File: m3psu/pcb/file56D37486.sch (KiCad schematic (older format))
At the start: 42 parts

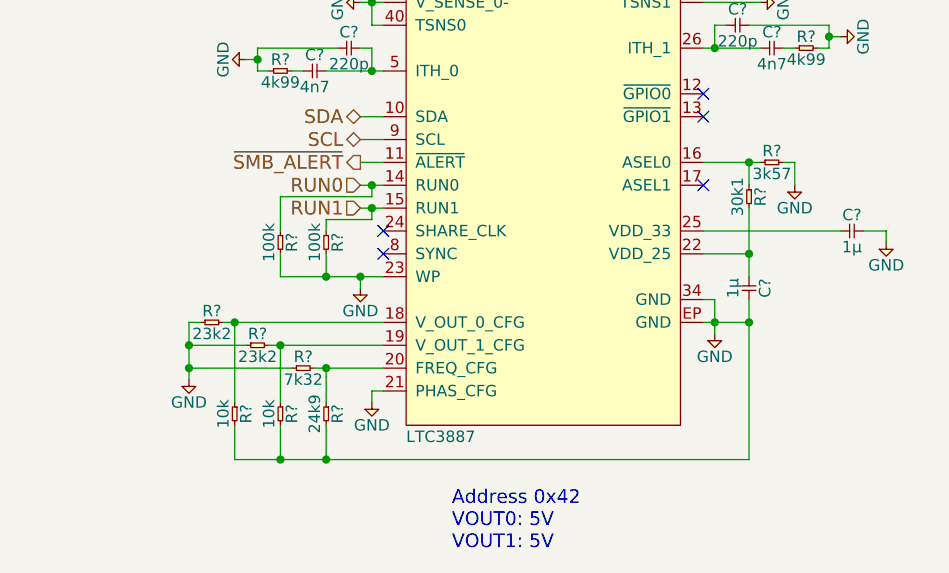
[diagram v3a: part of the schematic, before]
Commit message: Added current monitor and control for pyros. Modified DC/DC converters.
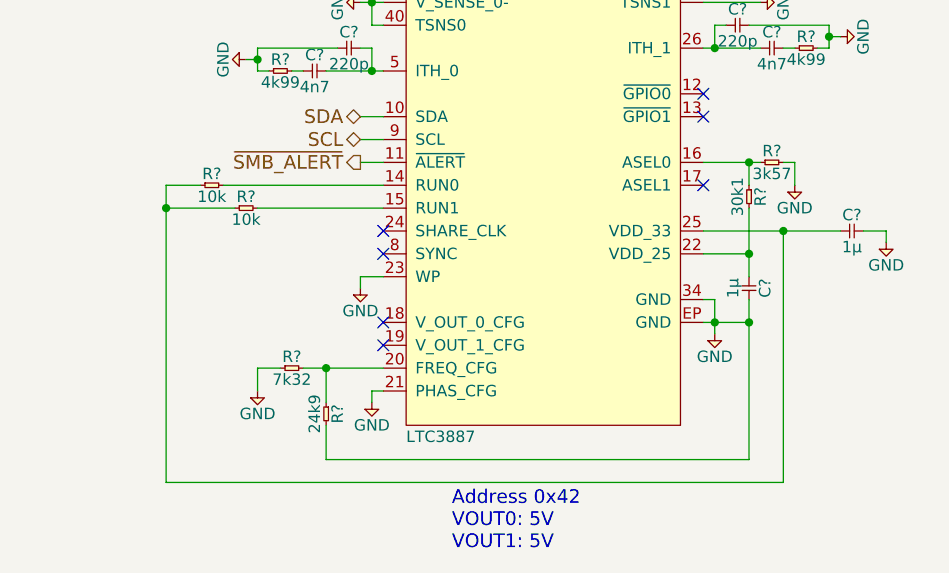
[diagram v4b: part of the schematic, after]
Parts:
- removed R?: 24k9, agg:0402, symbol R
- removed R? (x2): 10k, agg:0402, symbol R
- removed R? (x2): 23k2, agg:0402, symbol R
- removed R?: 7k32, agg:0402, symbol R
- removed R? (x2): 100k, agg:0402, symbol R
- added R?: 24k9, agg:0402, symbol R
- added R?: 7k32, agg:0402, symbol R
- added R? (x2): 10k, agg:0402, symbol R
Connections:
- net GND: now also R?.1, R?.2
- net at IC?.20 (FREQ_CFG): now also R?.1, R?.2
- net at C?.1, IC?.25 (VDD_33): now also R?.1, R?.1
- net RUN0: no longer names the net of IC?.14 (RUN0)
- net RUN0: now also R?.2
- net RUN1: no longer names the net of IC?.15 (RUN1)
- net RUN1: now also R?.2
- no-connect marks 5 -> 7
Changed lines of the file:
@@
 $Descr A4 11693 8268
 encoding utf-8
-Sheet 7 10
+Sheet 7 12
 Title ""
 Date ""
@@
 	1    0    0    -1
 $EndComp
-$Comp
-L R R?
-U 1 1 56D56E95
-P 4850 5300
-F 0 "R?" H 4900 5350 50  0000 C CNN
-F 1 "24k9" H 4900 5250 50  0000 C CNN
-F 2 "agg:0402" H 4850 5300 50  0001 C CNN
-F 3 "" H 4850 5300 50  0001 C CNN
-F 4 "1803690" H 4850 5300 60  0001 C CNN "Farnell"
-	1    4850 5300
-	0    1    1    0
-$EndComp
-$Comp
-L R R?
-U 1 1 56D56E9D
-P 4650 5300
-F 0 "R?" H 4700 5350 50  0000 C CNN
-F 1 "10k" H 4700 5250 50  0000 C CNN
-F 2 "agg:0402" H 4650 5300 50  0001 C CNN
-F 3 "" H 4650 5300 50  0001 C CNN
-F 4 "2447096" H 4650 5300 60  0001 C CNN "Farnell"
-	1    4650 5300
-	0    1    1    0
-$EndComp
-$Comp
-L R R?
-U 1 1 56D56EA5
-P 4450 5300
-F 0 "R?" H 4500 5350 50  0000 C CNN
-F 1 "10k" H 4500 5250 50  0000 C CNN
-F 2 "agg:0402" H 4450 5300 50  0001 C CNN
-F 3 "" H 4450 5300 50  0001 C CNN
-F 4 "2447096" H 4450 5300 60  0001 C CNN "Farnell"
-	1    4450 5300
-	0    1    1    0
-$EndComp
-$Comp
-L R R?
-U 1 1 56D56EAD
-P 4300 4950
-F 0 "R?" H 4350 5000 50  0000 C CNN
-F 1 "23k2" H 4350 4900 50  0000 C CNN
-F 2 "agg:0402" H 4300 4950 50  0001 C CNN
-F 3 "" H 4300 4950 50  0001 C CNN
-F 4 "2302774" H 4300 4950 60  0001 C CNN "Farnell"
-	1    4300 4950
-	1    0    0    -1
-$EndComp
-$Comp
-L R R?
-U 1 1 56D56EB5
-P 4500 5050
-F 0 "R?" H 4550 5100 50  0000 C CNN
-F 1 "23k2" H 4550 5000 50  0000 C CNN
-F 2 "agg:0402" H 4500 5050 50  0001 C CNN
-F 3 "" H 4500 5050 50  0001 C CNN
-F 4 "2302774" H 4500 5050 60  0001 C CNN "Farnell"
-	1    4500 5050
-	1    0    0    -1
-$EndComp
-$Comp
-L R R?
-U 1 1 56D56EBD
-P 4700 5150
-F 0 "R?" H 4750 5200 50  0000 C CNN
-F 1 "7k32" H 4750 5100 50  0000 C CNN
-F 2 "agg:0402" H 4700 5150 50  0001 C CNN
-F 3 "" H 4700 5150 50  0001 C CNN
-F 4 "2073231" H 4700 5150 60  0001 C CNN "Farnell"
-	1    4700 5150
-	1    0    0    -1
-$EndComp
-$Comp
-L GND #PWR?
-U 1 1 56D56EC4
-P 4250 5200
-F 0 "#PWR?" H 4120 5240 50  0001 L CNN
-F 1 "GND" H 4250 5100 50  0000 C CNN
-F 2 "" H 4250 5200 60  0000 C CNN
-F 3 "" H 4250 5200 60  0000 C CNN
-	1    4250 5200
-	1    0    0    -1
-$EndComp
 Text HLabel 5000 4050 0    60   BiDi ~ 0
 SDA
 Text HLabel 5000 4150 0    60   BiDi ~ 0
 SCL
-Text HLabel 5000 4350 0    60   Input ~ 0
-RUN0
-Text HLabel 5000 4450 0    60   Input ~ 0
-RUN1
 $Comp
 L GND #PWR?
@@
 	5000 3750 5050 3750
 Wire Wire Line
-	5050 4500 5050 4450
-Wire Wire Line
 	7050 3650 6700 3650
 Connection ~ 7050 3700
@@
 Wire Wire Line
 	6500 3750 6750 3750
-Connection ~ 5050 4450
-Connection ~ 5050 4350
-Wire Wire Line
-	5050 4400 5050 4350
 Wire Wire Line
 	5000 4150 5100 4150
 Wire Wire Line
 	5000 4050 5100 4050
-Wire Wire Line
-	5000 4350 5100 4350
-Wire Wire Line
-	5000 4450 5100 4450
 Wire Wire Line
 	6850 4250 6900 4250
@@
 	5000 4750 5000 4800
 Wire Wire Line
-	4650 4750 5100 4750
-Connection ~ 4250 5150
-Wire Wire Line
-	4250 5150 4700 5150
-Connection ~ 4250 5050
-Wire Wire Line
-	4500 5050 4250 5050
-Wire Wire Line
-	4250 4950 4250 5200
-Wire Wire Line
-	4300 4950 4250 4950
-Connection ~ 4850 5150
-Connection ~ 4650 5050
-Connection ~ 4450 4950
-Wire Wire Line
-	4400 4950 5100 4950
-Wire Wire Line
-	4450 5300 4450 4950
-Wire Wire Line
-	4600 5050 5100 5050
-Wire Wire Line
-	4650 5300 4650 5050
-Wire Wire Line
-	4800 5150 5100 5150
-Wire Wire Line
-	4850 5150 4850 5300
-Wire Wire Line
 	5050 5250 5100 5250
-Connection ~ 4850 5550
-Wire Wire Line
-	4850 5400 4850 5550
-Connection ~ 4650 5550
-Wire Wire Line
-	4650 5400 4650 5550
-Wire Wire Line
-	4450 5550 4450 5400
 Connection ~ 6700 4950
-Wire Wire Line
-	6700 5550 4450 5550
 Wire Wire Line
 	7200 4550 7300 4550
@@
 Text Notes 5400 5950 0    60   ~ 0
 Address 0x42\nVOUT0: 5V\nVOUT1: 5V
-$Comp
-L R R?
-U 1 1 56D56FDB
-P 4850 4550
-F 0 "R?" H 4900 4600 50  0000 C CNN
-F 1 "100k" H 4900 4500 50  0000 C CNN
-F 2 "agg:0402" H 4850 4550 50  0001 C CNN
-F 3 "" H 4850 4550 50  0001 C CNN
-F 4 "2447094" H 4850 4550 60  0001 C CNN "Farnell"
-	1    4850 4550
-	0    1    1    0
-$EndComp
-Wire Wire Line
-	4850 4750 4850 4650
-Connection ~ 5000 4750
-Wire Wire Line
-	5050 4500 4850 4500
-Wire Wire Line
-	4850 4500 4850 4550
-Wire Wire Line
-	5050 4400 4650 4400
-Wire Wire Line
-	4650 4400 4650 4550
-$Comp
-L R R?
-U 1 1 56D56FE9
-P 4650 4550
-F 0 "R?" H 4700 4600 50  0000 C CNN
-F 1 "100k" H 4700 4500 50  0000 C CNN
-F 2 "agg:0402" H 4650 4550 50  0001 C CNN
-F 3 "" H 4650 4550 50  0001 C CNN
-F 4 "2447094" H 4650 4550 60  0001 C CNN "Farnell"
-	1    4650 4550
-	0    1    1    0
-$EndComp
-Wire Wire Line
-	4650 4650 4650 4750
-Connection ~ 4850 4750
+Wire Wire Line
+	5000 4750 5100 4750
+$Comp
+L R R?
+U 1 1 56DDC75E
+P 4850 5300
+F 0 "R?" H 4900 5350 50  0000 C CNN
+F 1 "24k9" H 4900 5250 50  0000 C CNN
+F 2 "agg:0402" H 4850 5300 50  0001 C CNN
+F 3 "" H 4850 5300 50  0001 C CNN
+F 4 "1803690" H 4850 5300 60  0001 C CNN "Farnell"
+	1    4850 5300
+	0    1    1    0
+$EndComp
+$Comp
+L GND #PWR?
+U 1 1 56DDC765
+P 4550 5250
+F 0 "#PWR?" H 4420 5290 50  0001 L CNN
+F 1 "GND" H 4550 5150 50  0000 C CNN
+F 2 "" H 4550 5250 60  0000 C CNN
+F 3 "" H 4550 5250 60  0000 C CNN
+	1    4550 5250
+	1    0    0    -1
+$EndComp
+Connection ~ 4850 5150
+Wire Wire Line
+	4750 5150 5100 5150
+Wire Wire Line
+	4850 5150 4850 5300
+Wire Wire Line
+	4850 5400 4850 5550
+$Comp
+L R R?
+U 1 1 56DDC770
+P 4650 5150
+F 0 "R?" H 4700 5200 50  0000 C CNN
+F 1 "7k32" H 4700 5100 50  0000 C CNN
+F 2 "agg:0402" H 4650 5150 50  0001 C CNN
+F 3 "" H 4650 5150 50  0001 C CNN
+F 4 "2073231" H 4650 5150 60  0001 C CNN "Farnell"
+	1    4650 5150
+	1    0    0    -1
+$EndComp
+Wire Wire Line
+	4650 5150 4550 5150
+Wire Wire Line
+	4550 5150 4550 5250
+Wire Wire Line
+	4850 5550 6700 5550
+Wire Wire Line
+	4150 5650 6850 5650
+Wire Wire Line
+	4150 4350 4150 5650
+$Comp
+L R R?
+U 1 1 56DDC77D
+P 4300 4350
+F 0 "R?" H 4350 4400 50  0000 C CNN
+F 1 "10k" H 4350 4300 50  0000 C CNN
+F 2 "agg:0402" H 4300 4350 50  0001 C CNN
+F 3 "" H 4300 4350 50  0001 C CNN
+F 4 "2447096" H 4300 4350 60  0001 C CNN "Farnell"
+	1    4300 4350
+	1    0    0    -1
+$EndComp
+$Comp
+L R R?
+U 1 1 56DDC785
+P 4450 4450
+F 0 "R?" H 4500 4500 50  0000 C CNN
+F 1 "10k" H 4500 4400 50  0000 C CNN
+F 2 "agg:0402" H 4450 4450 50  0001 C CNN
+F 3 "" H 4450 4450 50  0001 C CNN
+F 4 "2447096" H 4450 4450 60  0001 C CNN "Farnell"
+	1    4450 4450
+	1    0    0    -1
+$EndComp
+Wire Wire Line
+	4150 4350 4300 4350
+Wire Wire Line
+	4450 4450 4150 4450
+Connection ~ 4150 4450
+Wire Wire Line
+	4400 4350 5100 4350
+Wire Wire Line
+	4550 4450 5100 4450
+Wire Wire Line
+	6850 5650 6850 4550
+Connection ~ 6850 4550
+NoConn ~ 5100 4950
+NoConn ~ 5100 5050
 $EndSCHEMATC

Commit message: Added footprints and datasheets to ALL transistors. Only 47uF capacitor has no footprint now.
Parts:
- removed Q? (x4): NFET, symbol NFET
- added Q? (x4): SiZ340DT, agg:PowerPair3x3, symbol SiZ340DT
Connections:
- net GND: now also Q?.S2, Q?.S2
- net VCC: now also Q?.D1 (S1D2), Q?.D1 (S1D2)
- net at C?.2, IC?.29 (SW1), L?.1: now also Q?.S1D2, Q?.S1D2
- net at IC?.30 (TG1): now also Q?.G1
- net at IC?.32 (BG1): now also Q?.G2
- net at IC?.36 (BG0): now also Q?.G2
- net at IC?.38 (TG0): now also Q?.G1
- net at C?.1, IC?.39 (SW0), L?.2: now also Q?.S1D2, Q?.S1D2
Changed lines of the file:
@@
-$EndComp
-$Comp
-L NFET Q?
-U 1 1 56D56D8B
-P 7150 2650
-F 0 "Q?" H 6900 2680 50  0000 L CNN
-F 1 "NFET" H 6900 2490 50  0000 L CNN
-F 2 "" H 7150 2650 50  0001 C CNN
-F 3 "" H 7150 2650 50  0001 C CNN
-F 4 "2422226" H 7150 2650 60  0001 C CNN "Farnell"
-	1    7150 2650
-	1    0    0    -1
-$EndComp
-$Comp
-L NFET Q?
-U 1 1 56D56D93
-P 7150 3050
-F 0 "Q?" H 6900 3080 50  0000 L CNN
-F 1 "NFET" H 6900 2890 50  0000 L CNN
-F 2 "" H 7150 3050 50  0001 C CNN
-F 3 "" H 7150 3050 50  0001 C CNN
-F 4 "2422226" H 7150 3050 60  0001 C CNN "Farnell"
-	1    7150 3050
-	1    0    0    -1
-$EndComp
-$Comp
-L NFET Q?
-U 1 1 56D56D9B
-P 4450 3050
-F 0 "Q?" H 4200 3080 50  0000 L CNN
-F 1 "NFET" H 4200 2890 50  0000 L CNN
-F 2 "" H 4450 3050 50  0001 C CNN
-F 3 "" H 4450 3050 50  0001 C CNN
-F 4 "2422226" H 4450 3050 60  0001 C CNN "Farnell"
-	1    4450 3050
-	-1   0    0    -1
-$EndComp
-$Comp
-L NFET Q?
-U 1 1 56D56DA3
-P 4450 2650
-F 0 "Q?" H 4200 2680 50  0000 L CNN
-F 1 "NFET" H 4200 2490 50  0000 L CNN
-F 2 "" H 4450 2650 50  0001 C CNN
-F 3 "" H 4450 2650 50  0001 C CNN
-F 4 "2422226" H 4450 2650 60  0001 C CNN "Farnell"
-	1    4450 2650
-	-1   0    0    -1
 $EndComp
 $Comp
@@
 NoConn ~ 5100 4950
 NoConn ~ 5100 5050
+$Comp
+L SiZ340DT Q?
+U 1 1 56E08906
+P 7150 2650
+AR Path="/56B7662E/56B76640/56E08906" Ref="Q?"  Part="1"
+AR Path="/56B7662E/56D37487/56E08906" Ref="Q?"  Part="1"
+F 0 "Q?" H 6900 2700 50  0000 L CNN
+F 1 "SiZ340DT" H 7200 2550 50  0000 L CNN
+F 2 "agg:PowerPair3x3" H 7150 2350 50  0001 C CNN
+F 3 "http://www.vishay.com/docs/62877/siz340dt.pdf" H 6900 2700 50  0001 C CNN
+F 4 "2422226" H 7100 2850 50  0001 C CNN "Farnell"
+	1    7150 2650
+	1    0    0    -1
+$EndComp
+$Comp
+L SiZ340DT Q?
+U 2 1 56E0890E
+P 7150 3050
+AR Path="/56B7662E/56B76640/56E0890E" Ref="Q?"  Part="2"
+AR Path="/56B7662E/56D37487/56E0890E" Ref="Q?"  Part="2"
+F 0 "Q?" H 6900 3100 50  0000 L CNN
+F 1 "SiZ340DT" H 7200 2950 50  0000 L CNN
+F 2 "agg:PowerPair3x3" H 7150 2750 50  0001 C CNN
+F 3 "http://www.vishay.com/docs/62877/siz340dt.pdf" H 6900 3100 50  0001 C CNN
+F 4 "2422226" H 7100 3250 50  0001 C CNN "Farnell"
+	2    7150 3050
+	1    0    0    -1
+$EndComp
+$Comp
+L SiZ340DT Q?
+U 1 1 56E08A62
+P 4450 2650
+AR Path="/56B7662E/56B76640/56E08A62" Ref="Q?"  Part="1"
+AR Path="/56B7662E/56D37487/56E08A62" Ref="Q?"  Part="1"
+F 0 "Q?" H 4200 2700 50  0000 L CNN
+F 1 "SiZ340DT" H 4500 2550 50  0000 L CNN
+F 2 "agg:PowerPair3x3" H 4450 2350 50  0001 C CNN
+F 3 "http://www.vishay.com/docs/62877/siz340dt.pdf" H 4200 2700 50  0001 C CNN
+F 4 "2422226" H 4400 2850 50  0001 C CNN "Farnell"
+	1    4450 2650
+	-1   0    0    -1
+$EndComp
+$Comp
+L SiZ340DT Q?
+U 2 1 56E08A6A
+P 4450 3050
+AR Path="/56B7662E/56B76640/56E08A6A" Ref="Q?"  Part="2"
+AR Path="/56B7662E/56D37487/56E08A6A" Ref="Q?"  Part="2"
+F 0 "Q?" H 4200 3100 50  0000 L CNN
+F 1 "SiZ340DT" H 4500 2950 50  0000 L CNN
+F 2 "agg:PowerPair3x3" H 4450 2750 50  0001 C CNN
+F 3 "http://www.vishay.com/docs/62877/siz340dt.pdf" H 4200 3100 50  0001 C CNN
+F 4 "2422226" H 4400 3250 50  0001 C CNN "Farnell"
+	2    4450 3050
+	-1   0    0    -1
+$EndComp
 $EndSCHEMATC

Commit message: Added in PSU for PSU. Updated README.md. Not sure what's this m3psu-rescue.lib is for...
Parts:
- C? (x3): footprint agg:0603 -> agg:0805; Farnell 2494232 -> 1907510
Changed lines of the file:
@@
 EESchema Schematic File Version 2
+LIBS:m3psu-rescue
 LIBS:agg-kicad
 LIBS:m3psu-cache
@@
 F 0 "C?" H 5850 2170 50  0000 C CNN
 F 1 "22µ" H 5850 2030 50  0000 C CNN
-F 2 "agg:0603" H 5800 2100 50  0001 C CNN
+F 2 "agg:0805" H 5800 2100 50  0001 C CNN
 F 3 "" H 5800 2100 50  0001 C CNN
-F 4 "2494232" H 5800 2100 60  0001 C CNN "Farnell"
+F 4 "1907510" H 5800 2100 60  0001 C CNN "Farnell"
 	1    5800 2100
 	0    1    1    0
@@
 F 0 "C?" H 7700 3070 50  0000 C CNN
 F 1 "22µ" H 7700 2930 50  0000 C CNN
-F 2 "agg:0603" H 7650 3000 50  0001 C CNN
+F 2 "agg:0805" H 7650 3000 50  0001 C CNN
 F 3 "" H 7650 3000 50  0001 C CNN
-F 4 "2494232" H 7650 3000 60  0001 C CNN "Farnell"
+F 4 "1907510" H 7650 3000 60  0001 C CNN "Farnell"
 	1    7650 3000
 	0    1    1    0
@@
 F 0 "C?" H 4000 3070 50  0000 C CNN
 F 1 "22µ" H 4000 2930 50  0000 C CNN
-F 2 "agg:0603" H 3950 3000 50  0001 C CNN
+F 2 "agg:0805" H 3950 3000 50  0001 C CNN
 F 3 "" H 3950 3000 50  0001 C CNN
-F 4 "2494232" H 3950 3000 60  0001 C CNN "Farnell"
+F 4 "1907510" H 3950 3000 60  0001 C CNN "Farnell"
 	1    3950 3000
 	0    1    1    0
